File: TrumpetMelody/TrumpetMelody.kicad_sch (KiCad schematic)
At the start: 80 parts, among them J1 USB_B_Micro, J2 Conn_01x05, J3 640456-3, J4 640456-3, SW1 SW_Push, U1 STM32F411RETx, U2 TLV62565DBVR, U3 MAX98357AETE_T, U4 MAX7375AXR805

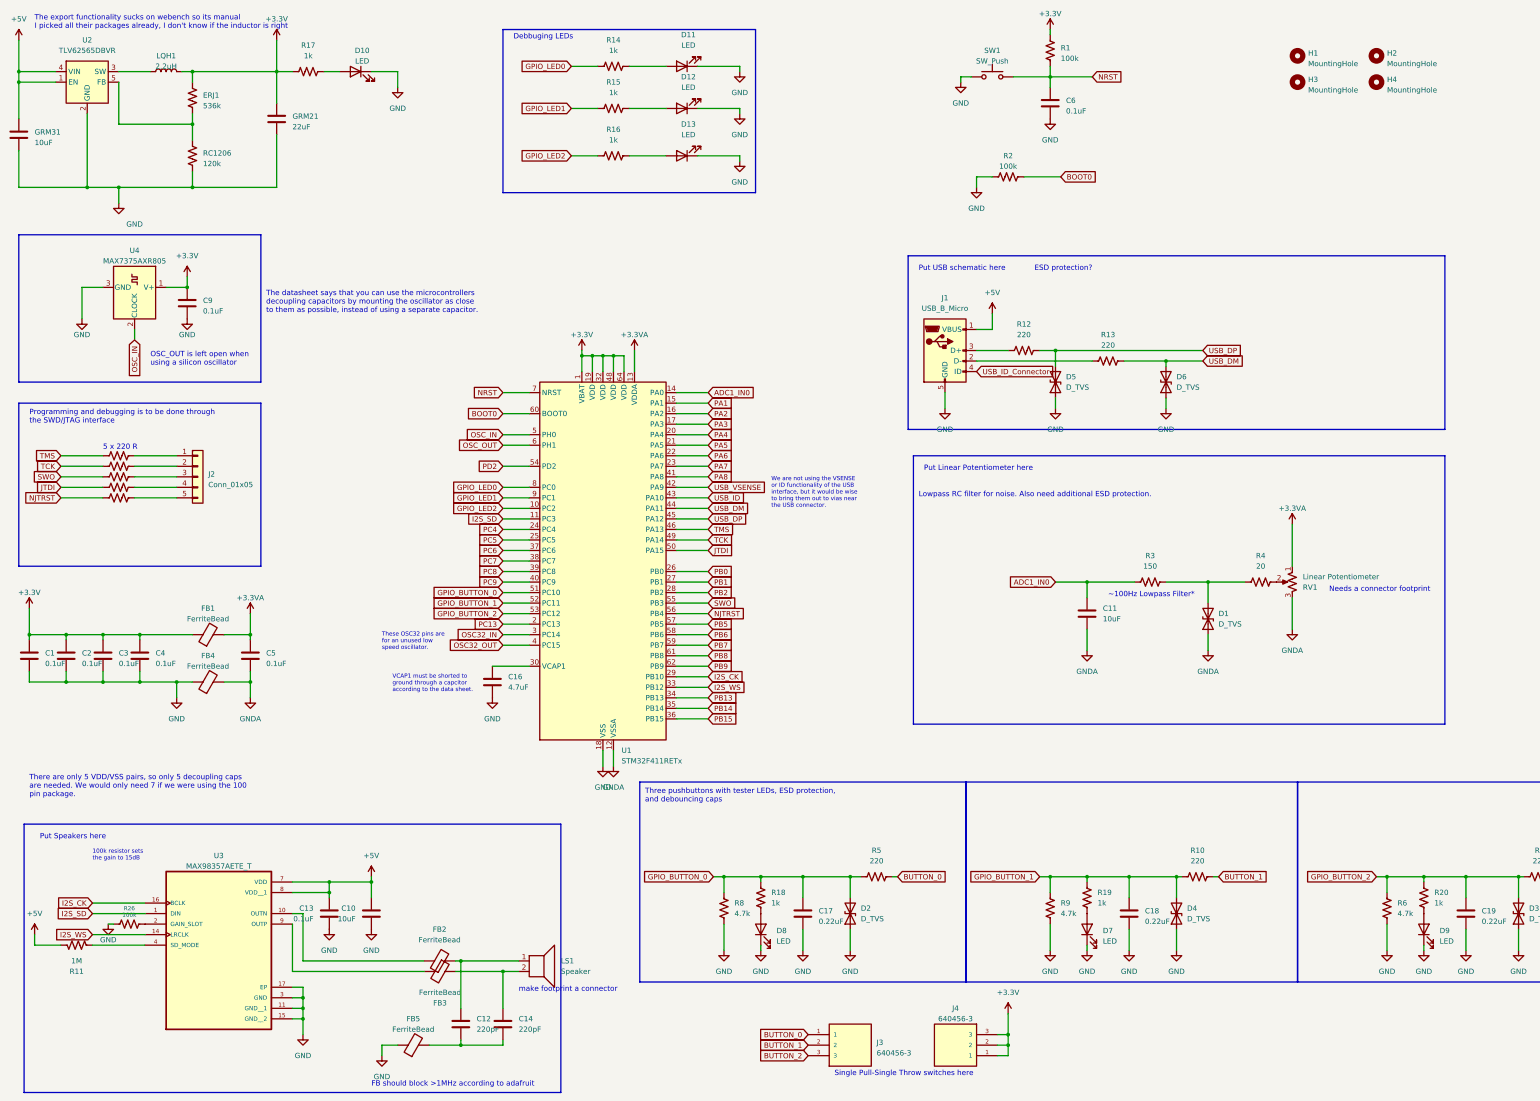
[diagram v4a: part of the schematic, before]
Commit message: Removed question marks from schematic
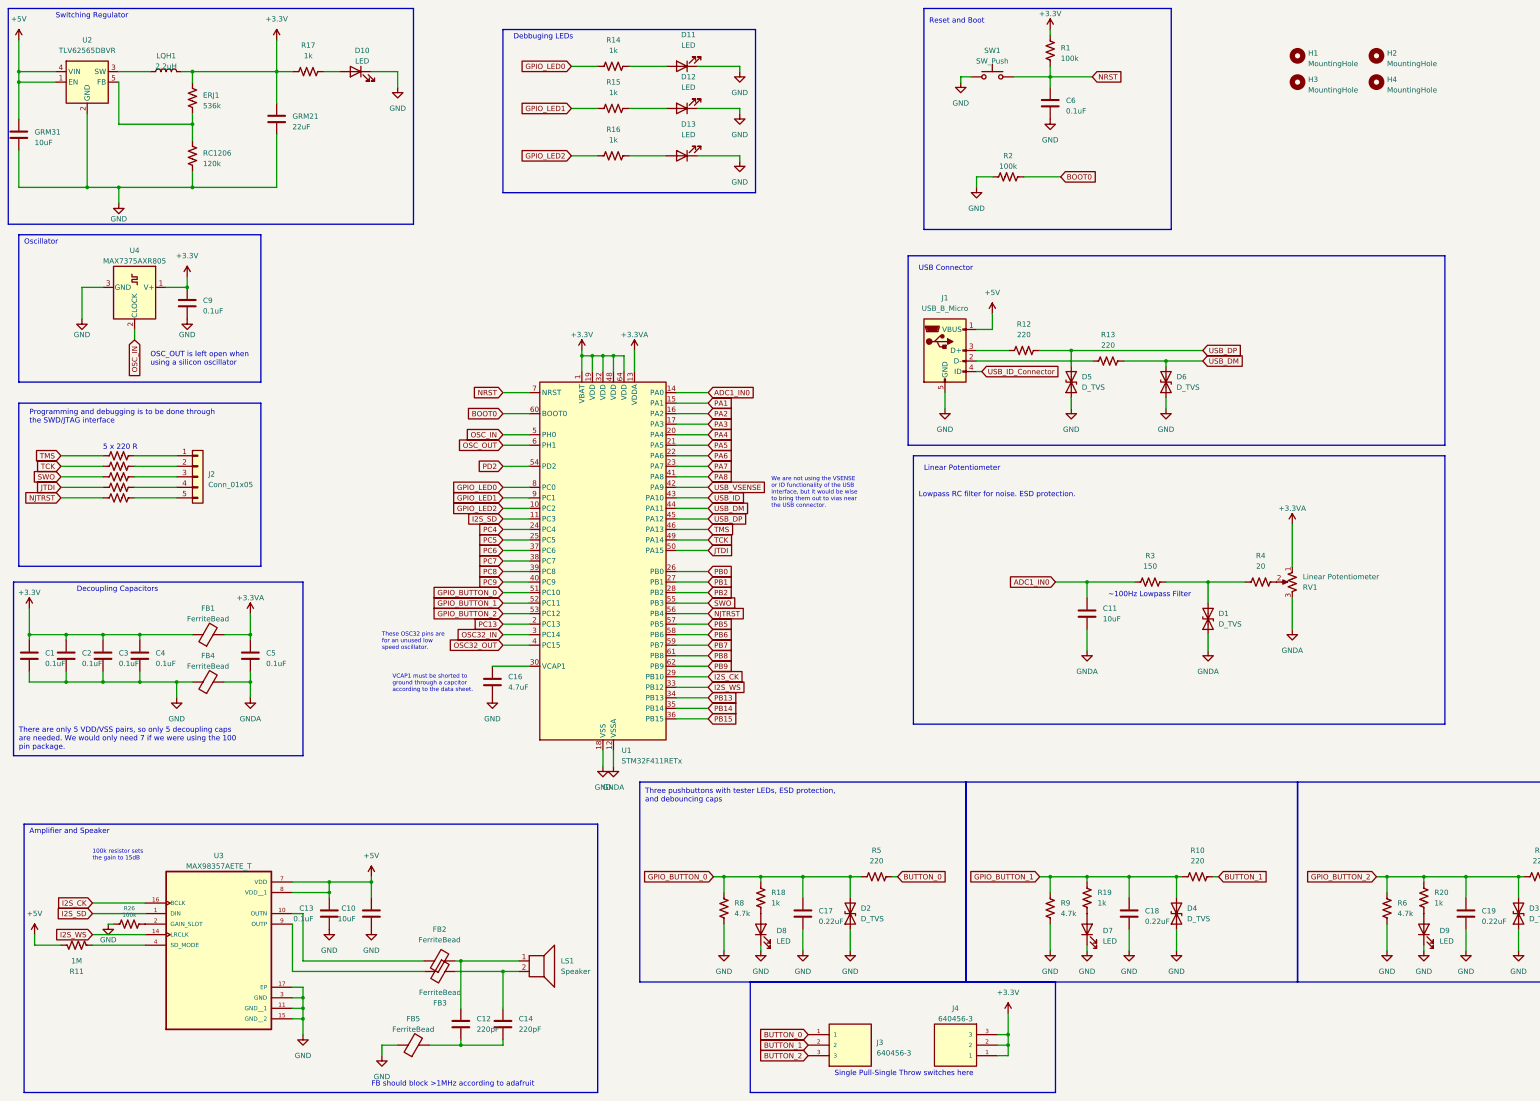
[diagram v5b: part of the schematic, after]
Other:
- note added: "Amplifier and Speaker"
- note added: "Decoupling Capacitors"
- note added: "Linear Potentiometer"
- note added: "Lowpass RC filter for noise. ESD protection."
- note added: "Oscillator"
- note added: "Reset and Boot"
- note added: "Switching Regulator"
- note added: "USB Connector"
- note added: "~100Hz Lowpass Filter"
- note removed: "ESD protection?"
- note removed: "Lowpass RC filter for noise. Also need additional ESD protection."
- note removed: "Needs a connector footprint"
- note removed: "Put Linear Potentiometer here"
- note removed: "Put Speakers here"
- note removed: "Put USB schematic here"
- note removed: "The datasheet says that you can use the microcontrollers decoupling capacitors by mounting the oscillator as close to them as possible, instead of using a separate capacitor."
- note removed: "The export functionality sucks on webench so its manual I picked all their packages already, I don't know if the inductor is right"
- note removed: "make footprint a connector"
- note removed: "~100Hz Lowpass Filter*"
- moved on the sheet: D5
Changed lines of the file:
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@@
 (kicad_sch (version 20230121) (generator eeschema)
   (paper "A3")
-  (junction (at 265.43 95.25) (diameter 0) (color 0 0 0 0)
-  )
   (junction (at 83.82 251.46) (diameter 0) (color 0 0 0 0)
   )
@@
   (junction (at 57.15 55.88) (diameter 0) (color 0 0 0 0)
   )
+  (junction (at 269.24 95.25) (diameter 0) (color 0 0 0 0)
+  )
   (junction (at 215.9 222.25) (diameter 0) (color 0 0 0 0)
   )
@@
     (stroke (width 0) (type default))
   )
-  (wire (pts (xy 265.43 95.25) (xy 265.43 99.06))
+  (wire (pts (xy 269.24 95.25) (xy 269.24 99.06))
+    (stroke (width 0) (type default))
+  )
+  (wire (pts (xy 269.24 95.25) (xy 300.99 95.25))
     (stroke (width 0) (type default))
   )
@@
     (stroke (width 0) (type default))
   )
-  (wire (pts (xy 265.43 95.25) (xy 300.99 95.25))
-    (stroke (width 0) (type default))
-  )
   (wire (pts (xy 156.21 191.77) (xy 156.21 195.58))
     (stroke (width 0) (type default))
@@
     (stroke (width 0) (type default))
   )
+  (wire (pts (xy 247.65 100.33) (xy 246.38 100.33))
+    (stroke (width 0) (type default))
+  )
   (wire (pts (xy 185.42 222.25) (xy 185.42 226.06))
     (stroke (width 0) (type default))
@@
     (stroke (width 0) (type default))
   )
-  (wire (pts (xy 261.62 95.25) (xy 265.43 95.25))
+  (wire (pts (xy 261.62 95.25) (xy 269.24 95.25))
     (stroke (width 0) (type default))
   )
@@
     (stroke (width 0) (type default))
   )
-  (wire (pts (xy 265.43 106.68) (xy 265.43 109.22))
+  (wire (pts (xy 269.24 106.68) (xy 269.24 109.22))
     (stroke (width 0) (type default))
   )
@@
     (stroke (width 0) (type default))
   )
-  (rectangle (start 229.87 72.39) (end 359.41 114.3)
+  (rectangle (start 229.87 72.39) (end 359.41 118.11)
     (stroke (width 0) (type default))
     (fill (type none))
@@
     (fill (type none))
   )
+  (rectangle (start 191.77 247.65) (end 265.43 274.32)
+    (stroke (width 0) (type default))
+    (fill (type none))
+  )
+  (rectangle (start 12.7 12.7) (end 110.49 64.77)
+    (stroke (width 0) (type default))
+    (fill (type none))
+  )
   (rectangle (start 165.1 199.39) (end 243.84 247.65)
     (stroke (width 0) (type default))
     (fill (type none))
   )
+  (rectangle (start 13.97 151.13) (end 83.82 193.04)
+    (stroke (width 0) (type default))
+    (fill (type none))
+  )
   (rectangle (start 15.24 107.95) (end 73.66 147.32)
     (stroke (width 0) (type default))
     (fill (type none))
   )
+  (rectangle (start 233.68 12.7) (end 293.37 66.04)
+    (stroke (width 0) (type default))
+    (fill (type none))
+  )
   (rectangle (start 323.85 199.39) (end 406.4 247.65)
     (stroke (width 0) (type default))
@@
     (fill (type none))
   )
-  (rectangle (start 16.51 209.55) (end 146.05 274.32)
+  (rectangle (start 16.51 209.55) (end 154.94 274.32)
     (stroke (width 0) (type default))
     (fill (type none))
@@
     (fill (type none))
   )
-  (text "Needs a connector footprint" (at 331.47 153.67 0)
+  (text "USB Connector" (at 232.41 76.2 0)
     (effects (font (size 1.27 1.27)) (justify left bottom))
   )
-  (text "The datasheet says that you can use the microcontrollers \ndecoupling capacitors by mounting the oscillator as close \nto them as possible, instead of using a separate capacitor."
-    (at 74.93 86.36 0)
+  (text "Switching Regulator" (at 24.13 15.24 0)
     (effects (font (size 1.27 1.27)) (justify left bottom))
   )
-  (text "Put Speakers here" (at 20.32 213.36 0)
+  (text "~100Hz Lowpass Filter" (at 278.13 154.94 0)
     (effects (font (size 1.27 1.27)) (justify left bottom))
   )
-  (text "Put USB schematic here" (at 232.41 76.2 0)
-    (effects (font (size 1.27 1.27)) (justify left bottom))
-  )
-  (text "~100Hz Lowpass Filter*" (at 278.13 154.94 0)
+  (text "5 x 220 R" (at 35.56 119.38 0)
     (effects (font (size 1.27 1.27)) (justify left bottom))
   )
-  (text "5 x 220 R" (at 35.56 119.38 0)
+  (text "Oscillator" (at 16.51 69.85 0)
     (effects (font (size 1.27 1.27)) (justify left bottom))
   )
@@
     (effects (font (size 1 1)) (justify left bottom))
   )
+  (text "Amplifier and Speaker" (at 17.78 212.09 0)
+    (effects (font (size 1.27 1.27)) (justify left bottom))
+  )
   (text "There are only 5 VDD/VSS pairs, so only 5 decoupling caps\nare needed. We would only need 7 if we were using the 100\npin package."
-    (at 17.78 203.2 0)
+    (at 15.24 191.77 0)
     (effects (font (size 1.27 1.27)) (justify left bottom))
   )
@@
     (effects (font (size 1.27 1.27)) (justify left bottom))
   )
-  (text "Put Linear Potentiometer here" (at 233.68 124.46 0)
-    (effects (font (size 1.27 1.27)) (justify left bottom))
-  )
-  (text "ESD protection?" (at 260.35 76.2 0)
+  (text "Linear Potentiometer" (at 233.68 124.46 0)
     (effects (font (size 1.27 1.27)) (justify left bottom))
   )
@@
     (effects (font (size 1.27 1.27)) (justify left bottom))
   )
-  (text "The export functionality sucks on webench so its manual\nI picked all their packages already, I don't know if the inductor is right"
-    (at 19.05 17.78 0)
-    (effects (font (size 1.27 1.27)) (justify left bottom))
-  )
-  (text "make footprint a connector" (at 135.89 250.19 0)
+  (text "Reset and Boot" (at 234.95 16.51 0)
     (effects (font (size 1.27 1.27)) (justify left bottom))
   )
@@
     (effects (font (size 1 1)) (justify left bottom))
   )
-  (text "Lowpass RC filter for noise. Also need additional ESD protection."
-    (at 232.41 130.81 0)
+  (text "Lowpass RC filter for noise. ESD protection." (at 232.41 130.81 0)
+    (effects (font (size 1.27 1.27)) (justify left bottom))
+  )
+  (text "Decoupling Capacitors" (at 29.21 153.67 0)
     (effects (font (size 1.27 1.27)) (justify left bottom))
   )
@@
     )
   )
-  (global_label "USB_ID_Connector" (shape input) (at 246.38 100.33 0) (fields_autoplaced)
+  (global_label "USB_ID_Connector" (shape input) (at 247.65 100.33 0) (fields_autoplaced)
     (effects (font (size 1.27 1.27)) (justify left))
-    (property "Intersheetrefs" "${INTERSHEET_REFS}" (at 265.8067 100.33 0)
+    (property "Intersheetrefs" "${INTERSHEET_REFS}" (at 267.0767 100.33 0)
       (effects (font (size 1.27 1.27)) (justify left) hide)
     )
@@
     )
   )
-  (symbol (lib_id "power:GND") (at 265.43 109.22 0) (unit 1)
+  (symbol (lib_id "power:GND") (at 269.24 109.22 0) (unit 1)
     (in_bom yes) (on_board yes) (dnp no) (fields_autoplaced)
-    (property "Reference" "#PWR039" (at 265.43 115.57 0)
+    (property "Reference" "#PWR039" (at 269.24 115.57 0)
       (effects (font (size 1.27 1.27)) hide)
     )
-    (property "Value" "GND" (at 265.43 114.3 0)
+    (property "Value" "GND" (at 269.24 114.3 0)
       (effects (font (size 1.27 1.27)))
     )
-    (property "Footprint" "" (at 265.43 109.22 0)
+    (property "Footprint" "" (at 269.24 109.22 0)
       (effects (font (size 1.27 1.27)) hide)
     )
-    (property "Datasheet" "" (at 265.43 109.22 0)
+    (property "Datasheet" "" (at 269.24 109.22 0)
       (effects (font (size 1.27 1.27)) hide)
     )
@@
     )
   )
-  (symbol (lib_id "Device:D_TVS") (at 265.43 102.87 90) (unit 1)
+  (symbol (lib_id "Device:D_TVS") (at 269.24 102.87 90) (unit 1)
     (in_bom yes) (on_board yes) (dnp no) (fields_autoplaced)
-    (property "Reference" "D5" (at 267.97 101.6 90)
+    (property "Reference" "D5" (at 271.78 101.6 90)
       (effects (font (size 1.27 1.27)) (justify right))
     )
-    (property "Value" "D_TVS" (at 267.97 104.14 90)
+    (property "Value" "D_TVS" (at 271.78 104.14 90)
       (effects (font (size 1.27 1.27)) (justify right))
     )
-    (property "Footprint" "Diode_SMD:D_0805_2012Metric" (at 265.43 102.87 0)
+    (property "Footprint" "Diode_SMD:D_0805_2012Metric" (at 269.24 102.87 0)
       (effects (font (size 1.27 1.27)) hide)
     )
-    (property "Datasheet" "~" (at 265.43 102.87 0)
+    (property "Datasheet" "~" (at 269.24 102.87 0)
       (effects (font (size 1.27 1.27)) hide)
     )
@@
       (effects (font (size 1.27 1.27)) hide)
     )
-    (property "Value" "GND" (at 43.18 64.77 0)
+    (property "Value" "GND" (at 39.37 63.5 0)
       (effects (font (size 1.27 1.27)))
     )

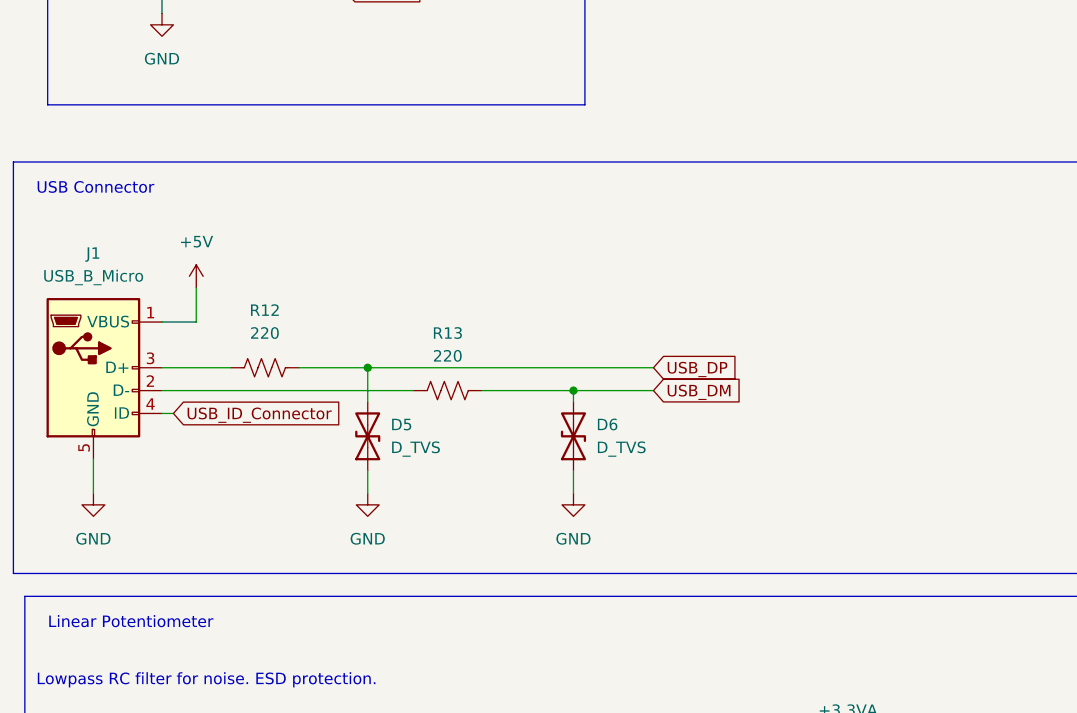
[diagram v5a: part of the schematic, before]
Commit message: New ESD protection on USB and verified
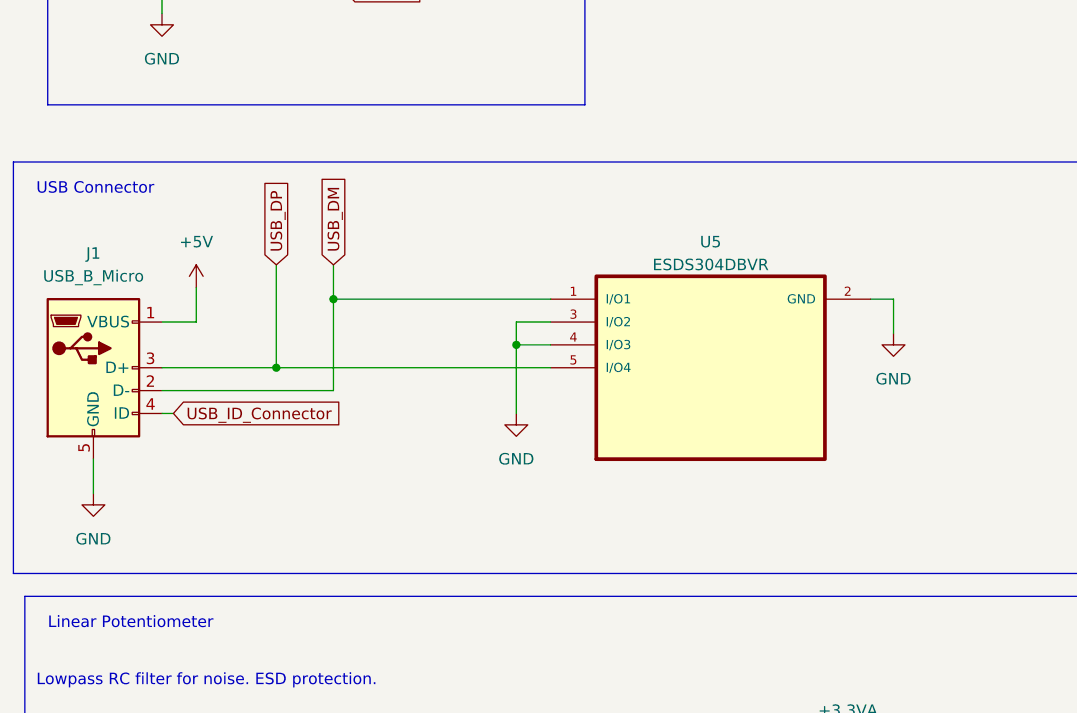
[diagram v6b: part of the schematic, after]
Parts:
- removed D5, D6: D_TVS, Diode_SMD:D_0805_2012Metric, symbol Device:D_TVS
- removed R12, R13: 220, Resistor_SMD:R_0805_2012Metric_Pad1.20x1.40mm_HandSolder, symbol Device:R_US
- added U5: ESDS304DBVR, TrumpetMelodyFootprintLibrary:SOT95P280X145-5N, symbol TrumpetMelody_Symbol_Library:ESDS304DBVR
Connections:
- net GND: now also U5.2 (GND), U5.3 (I/O2), U5.4 (I/O3)
- net USB_DM: now also J1.2 (D-), U5.1 (I/O1)
- net USB_DP: now also J1.3 (D+), U5.5 (I/O4)
